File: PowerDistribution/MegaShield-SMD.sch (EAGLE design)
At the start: 37 parts, among them IC1 TLE5206-2G, IC2 TLE5206-2G, IC3 TLE5206-2G, J10 DCJ0202

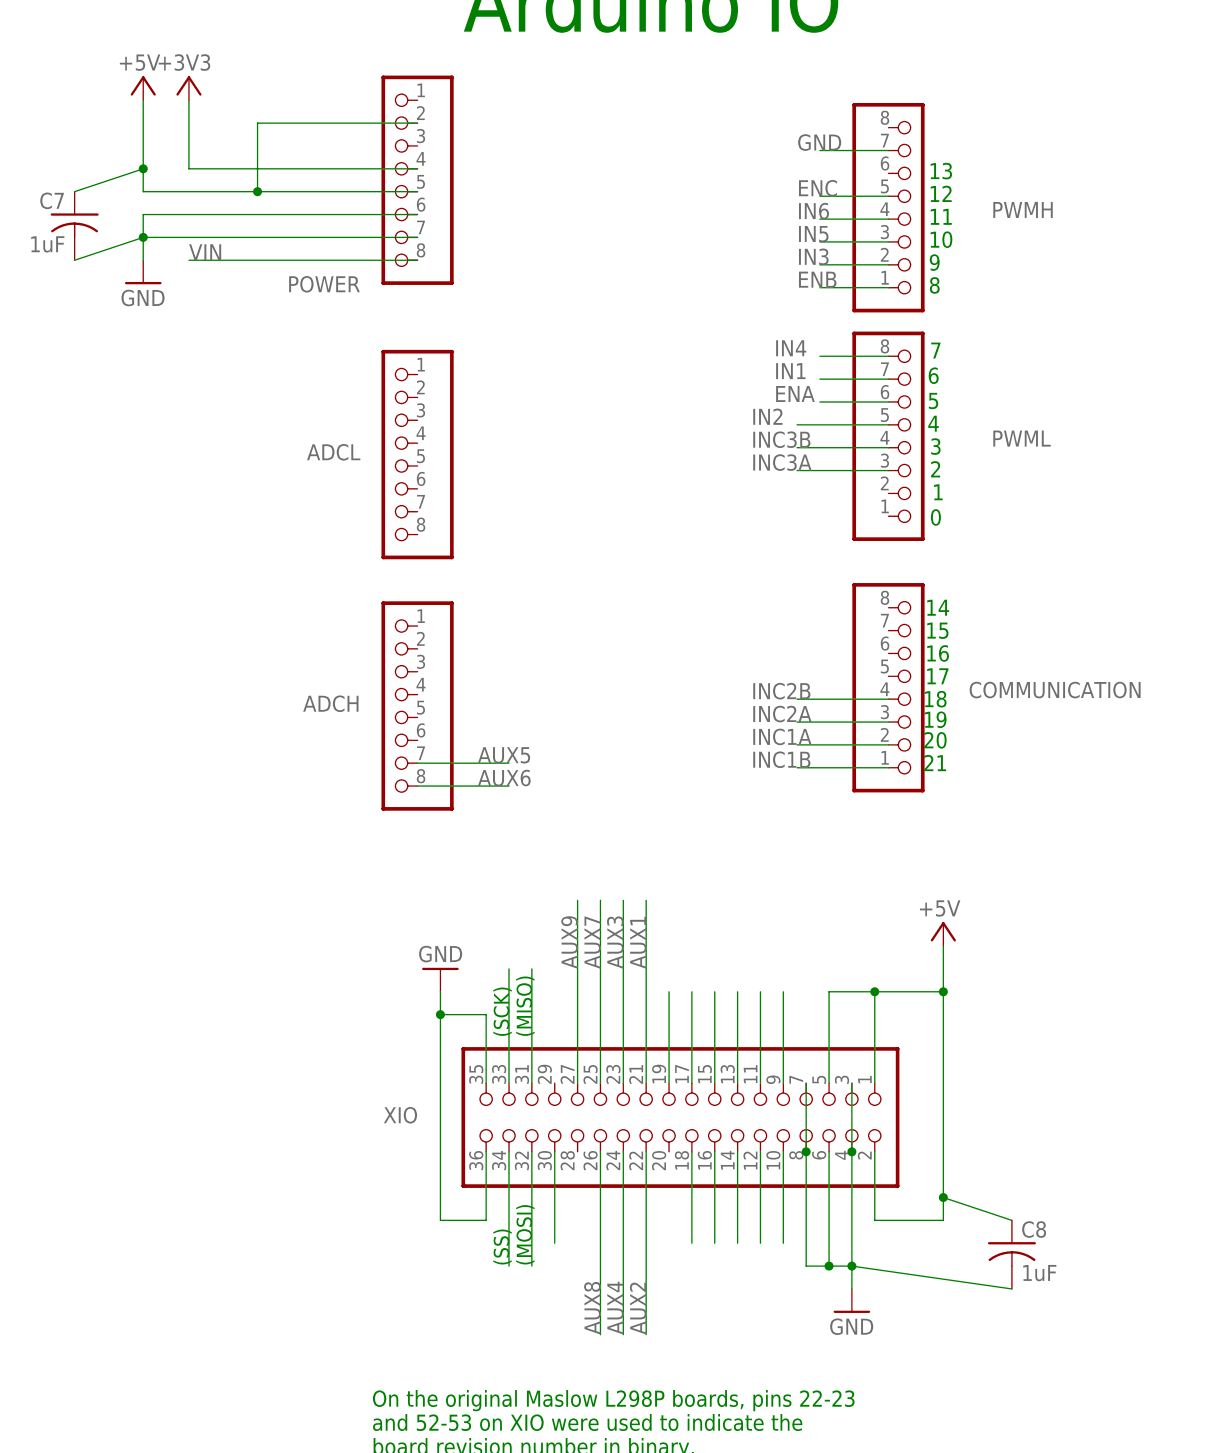
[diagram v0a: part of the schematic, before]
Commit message: Move caps on schematic, change colors in SMD .brd
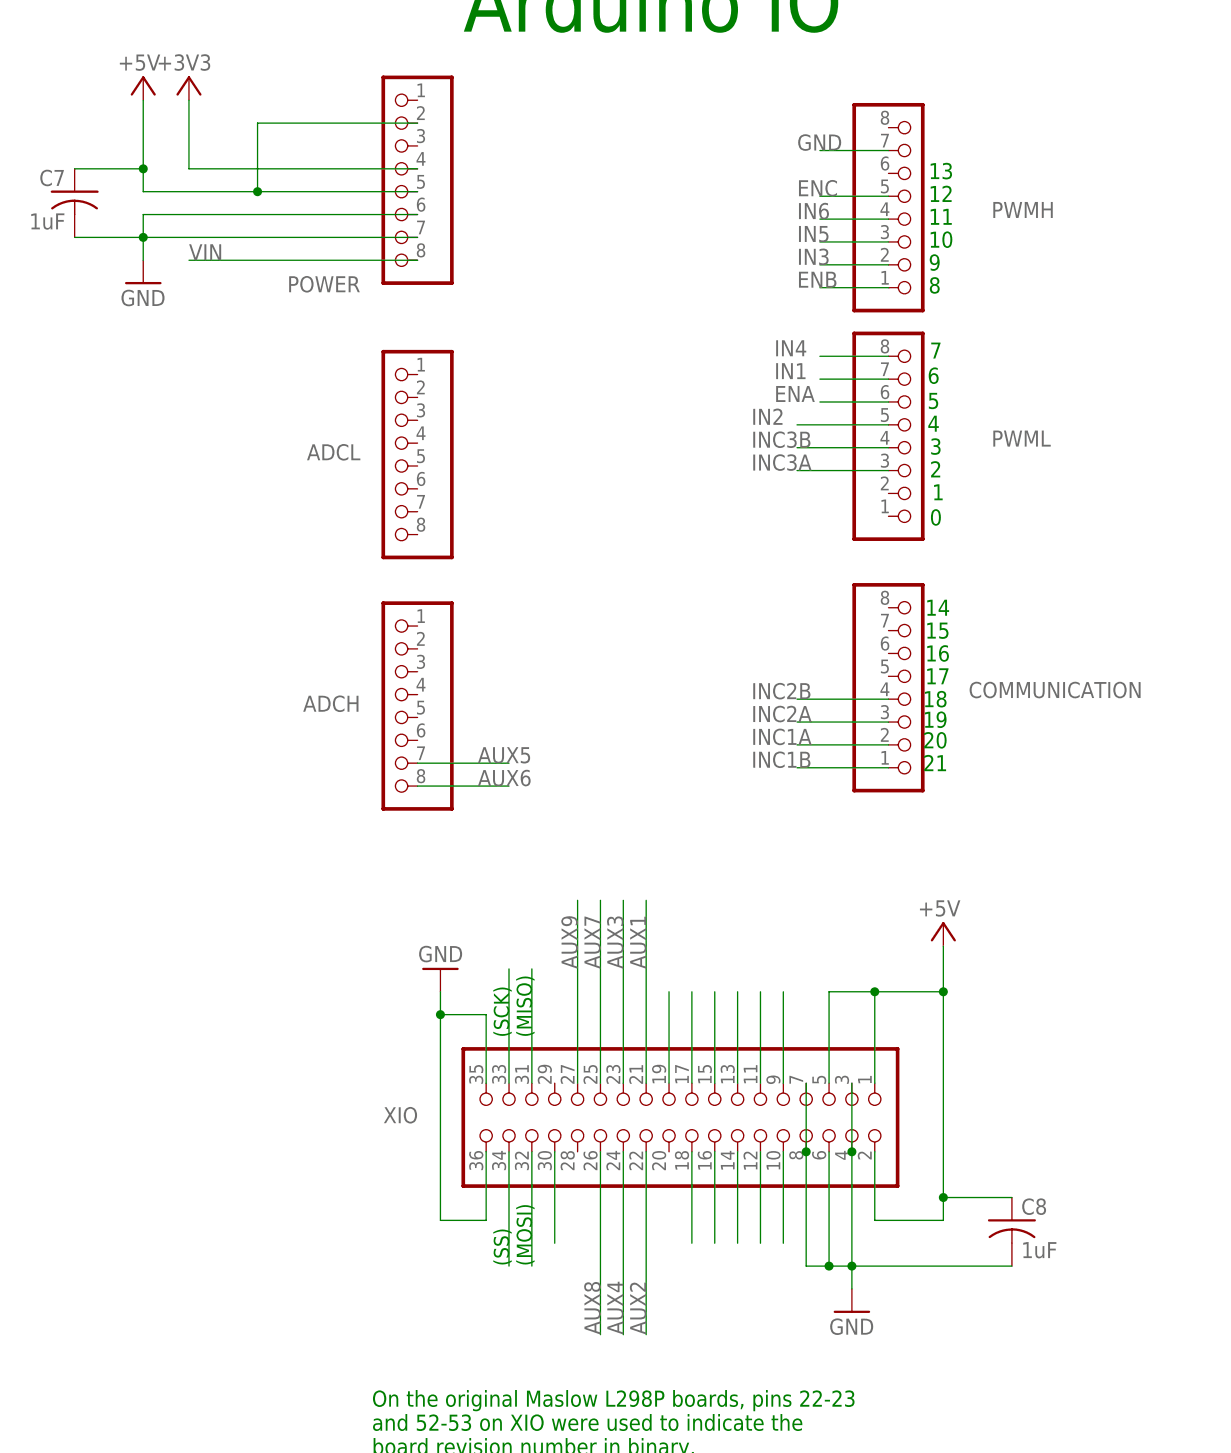
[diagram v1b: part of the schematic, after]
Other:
- moved on the sheet: C7, C8
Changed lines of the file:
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@@
 <attribute name="VALUE" x="157.48" y="172.72" size="1.778" layer="96"/>
 </instance>
-<instance part="C7" gate="G$1" x="20.32" y="236.22" rot="MR0"/>
-<instance part="C8" gate="G$1" x="124.46" y="121.92"/>
+<instance part="C7" gate="G$1" x="20.32" y="238.76" rot="MR0"/>
+<instance part="C8" gate="G$1" x="124.46" y="124.46"/>
 </instances>
 <busses>
@@
 <pinref part="POWER" gate="A" pin="7"/>
 <pinref part="C7" gate="G$1" pin="2"/>
-<wire x1="27.94" y1="233.68" x2="20.32" y2="231.14" width="0.1524" layer="91"/>
+<wire x1="27.94" y1="233.68" x2="20.32" y2="233.68" width="0.1524" layer="91"/>
 </segment>
 <segment>
@@
 <junction x="106.68" y="132.08"/>
 <pinref part="C8" gate="G$1" pin="2"/>
-<wire x1="106.68" y1="119.38" x2="124.46" y2="116.84" width="0.1524" layer="91"/>
+<wire x1="106.68" y1="119.38" x2="124.46" y2="119.38" width="0.1524" layer="91"/>
 <wire x1="101.6" y1="132.08" x2="101.6" y2="119.38" width="0.1524" layer="91"/>
 <pinref part="XIO" gate="A" pin="8"/>
@@
 <junction x="109.22" y="149.86"/>
 <pinref part="C8" gate="G$1" pin="1"/>
-<wire x1="124.46" y1="124.46" x2="116.84" y2="127" width="0.1524" layer="91"/>
+<wire x1="124.46" y1="127" x2="116.84" y2="127" width="0.1524" layer="91"/>
 <junction x="116.84" y="127"/>
 </segment>
@@
 <pinref part="POWER" gate="A" pin="2"/>
 <pinref part="C7" gate="G$1" pin="1"/>
-<wire x1="27.94" y1="241.3" x2="20.32" y2="238.76" width="0.1524" layer="91"/>
+<wire x1="27.94" y1="241.3" x2="20.32" y2="241.3" width="0.1524" layer="91"/>
 <junction x="27.94" y="241.3"/>
 </segment>
